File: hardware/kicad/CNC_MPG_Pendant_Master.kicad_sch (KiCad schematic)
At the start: 9 parts, among them J1 Buttons harness - planned con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, J2 Separate AUX stop status (opt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, J3 USB-C panel extension / USB2, SW8 E-STOP NC independent safety, U1 Seeed XIAO ESP32-S3, U2 MCP23017 breakout 0x20

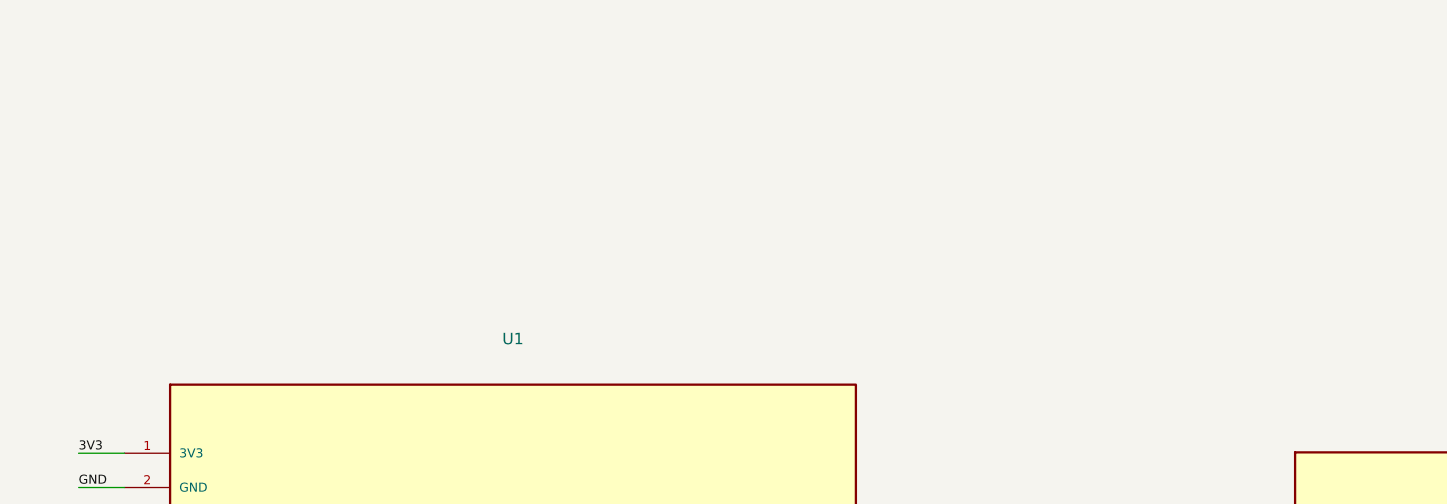
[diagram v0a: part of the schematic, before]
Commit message: hardware(kicad): annotate connected nets and point to wiring pinout schedule
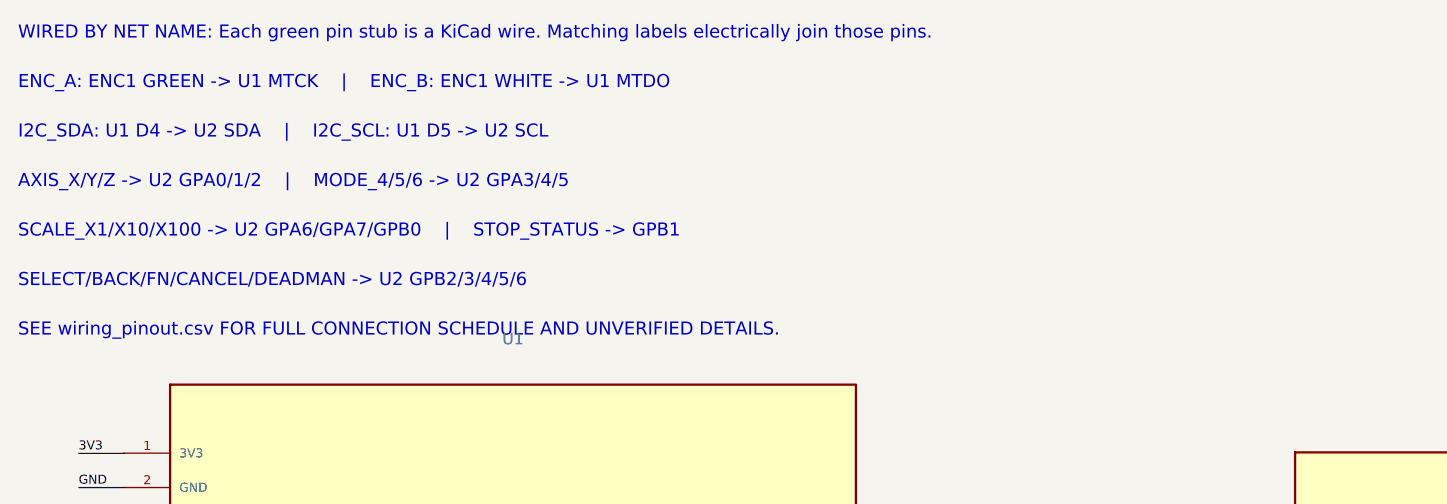
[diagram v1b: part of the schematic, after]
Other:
- note added: "AXIS_X/Y/Z -> U2 GPA0/1/2 | MODE_4/5/6 -> U2 GPA3/4/5"
- note added: "ENC_A: ENC1 GREEN -> U1 MTCK | ENC_B: ENC1 WHITE -> U1 MTDO"
- note added: "I2C_SDA: U1 D4 -> U2 SDA | I2C_SCL: U1 D5 -> U2 SCL"
- note added: "SCALE_X1/X10/X100 -> U2 GPA6/GPA7/GPB0 | STOP_STATUS -> GPB1"
- note added: "SEE wiring_pinout.csv FOR FULL CONNECTION SCHEDULE AND UNVERIFIED DETAILS."
- note added: "SELECT/BACK/FN/CANCEL/DEADMAN -> U2 GPB2/3/4/5/6"
- note added: "WIRED BY NET NAME: Each green pin stub is a KiCad wire. Matching labels electrically join those pins."
- title: CNC MPG Pendant - Master Component and Wiring Inventory -> CNC MPG Pendant - Connected Net Wiring Master

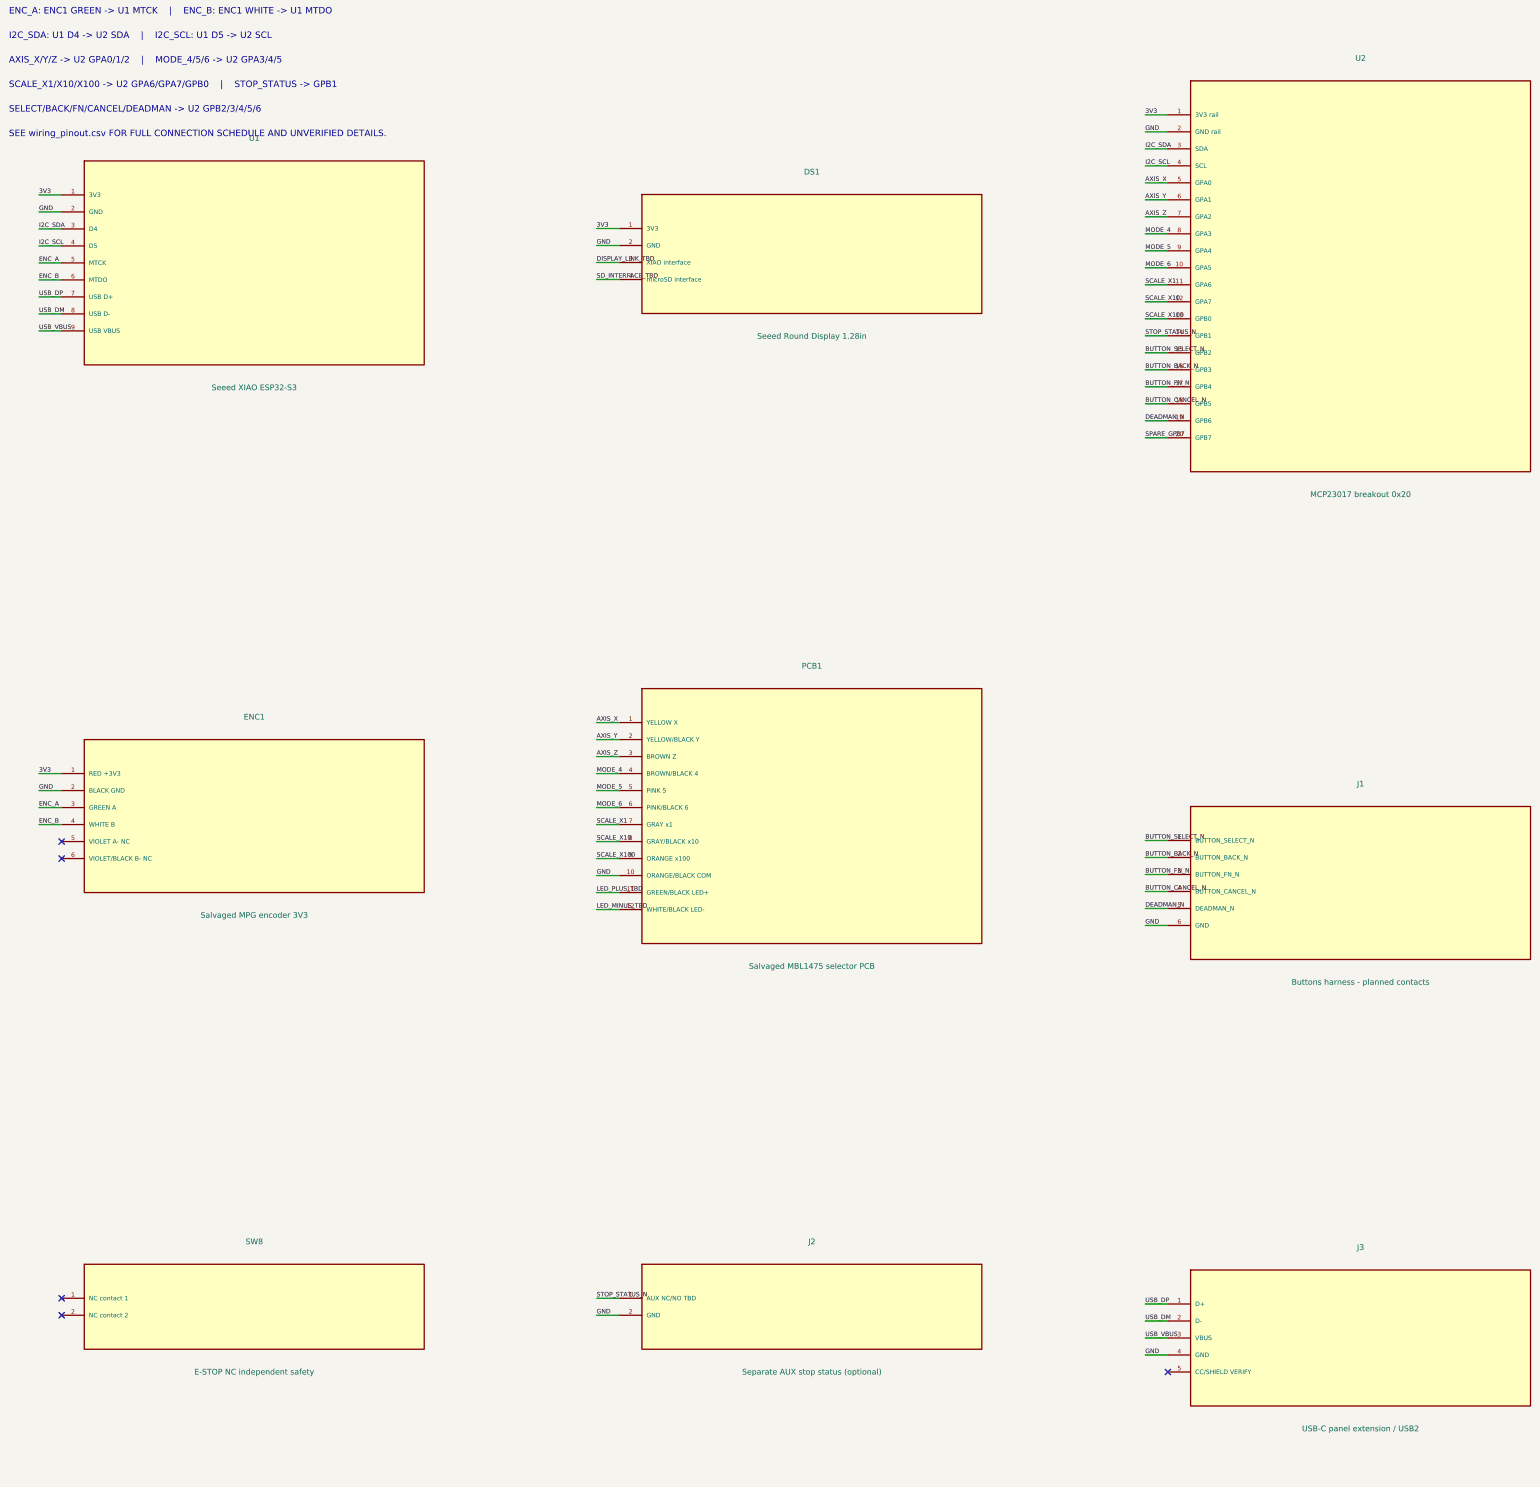
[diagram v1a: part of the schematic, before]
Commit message: fix(kicad): snap symbol pin positions, placements, wire endpoints and labels to 50 mil grid
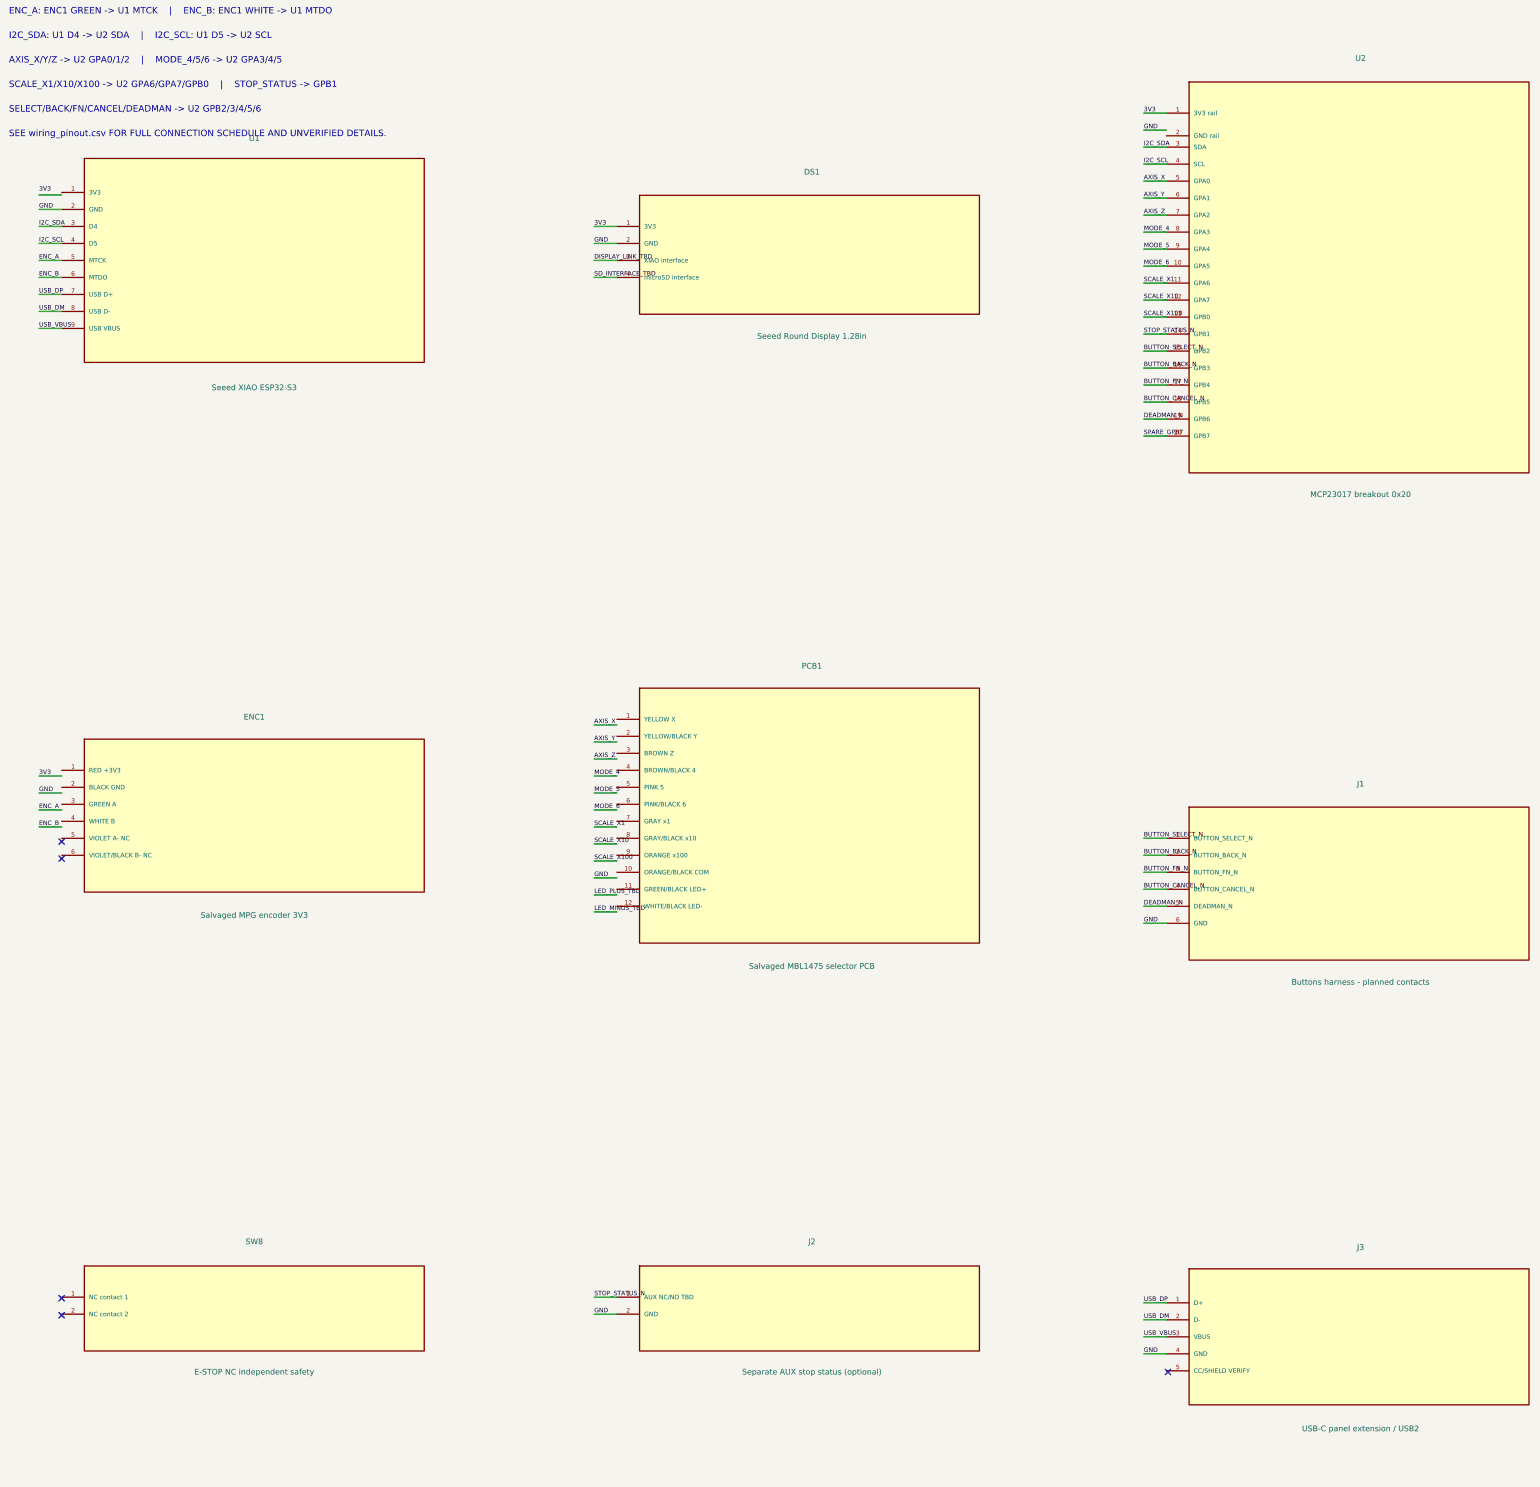
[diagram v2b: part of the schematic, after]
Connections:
- net 3V3: no longer ENC1.1 (RED +3V3), U1.1 (3V3)
- net AXIS_X: no longer PCB1.1 (YELLOW X)
- net AXIS_Y: no longer PCB1.2 (YELLOW/BLACK Y)
- net AXIS_Z: no longer PCB1.3 (BROWN Z)
- net ENC_A: no longer ENC1.3 (GREEN A)
- net ENC_B: no longer ENC1.4 (WHITE B)
- net GND: no longer ENC1.2 (BLACK GND), PCB1.10 (ORANGE/BLACK COM), U2.2 (GND rail)
- net LED_MINUS_TBD: no longer PCB1.12 (WHITE/BLACK LED-)
- net LED_PLUS_TBD: no longer PCB1.11 (GREEN/BLACK LED+)
- net MODE_4: no longer PCB1.4 (BROWN/BLACK 4)
- net MODE_5: no longer PCB1.5 (PINK 5)
- net MODE_6: no longer PCB1.6 (PINK/BLACK 6)
- net SCALE_X1: no longer PCB1.7 (GRAY x1)
- net SCALE_X10: no longer PCB1.8 (GRAY/BLACK x10)
- net SCALE_X100: no longer PCB1.9 (ORANGE x100)
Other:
- moved on the sheet: DS1, J2, PCB1, U1

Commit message: hardware(kicad): update CNC MPG pendant schematic
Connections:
- net 3V3: now also ENC1.1 (RED_+3V3), U1.1 (3V3)
- net AXIS_X: now also PCB1.1 (YELLOW_X)
- net AXIS_Y: now also PCB1.2 (YELLOW/BLACK_Y)
- net AXIS_Z: now also PCB1.3 (BROWN_Z)
- net ENC_A: now also ENC1.3 (GREEN_A)
- net ENC_B: now also ENC1.4 (WHITE_B)
- net GND: now also ENC1.2 (BLACK_GND), PCB1.10 (ORANGE/BLACK_COM), U2.2 (GND_rail)
- net LED_MINUS_TBD: now also PCB1.12 (WHITE/BLACK_LED-)
- net LED_PLUS_TBD: now also PCB1.11 (GREEN/BLACK_LED+)
- net MODE_4: now also PCB1.4 (BROWN/BLACK_4)
- net MODE_5: now also PCB1.5 (PINK_5)
- net MODE_6: now also PCB1.6 (PINK/BLACK_6)
- net SCALE_X1: now also PCB1.7 (GRAY_x1)
- net SCALE_X10: now also PCB1.8 (GRAY/BLACK_x10)
- net SCALE_X100: now also PCB1.9 (ORANGE_x100)
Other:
- moved on the sheet: DS1, ENC1, J1, J2, J3, PCB1, SW8, U1, U2
